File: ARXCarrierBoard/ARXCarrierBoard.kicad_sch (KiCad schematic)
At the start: 24 parts, among them J1 Conn_01x02_Male, J2 Conn_01x03_Male, J3 Conn_02x04_Male, J4 USB_B, SW2 SW_SPST, U2 SeeeduinoXIAO, U3 MAX3485

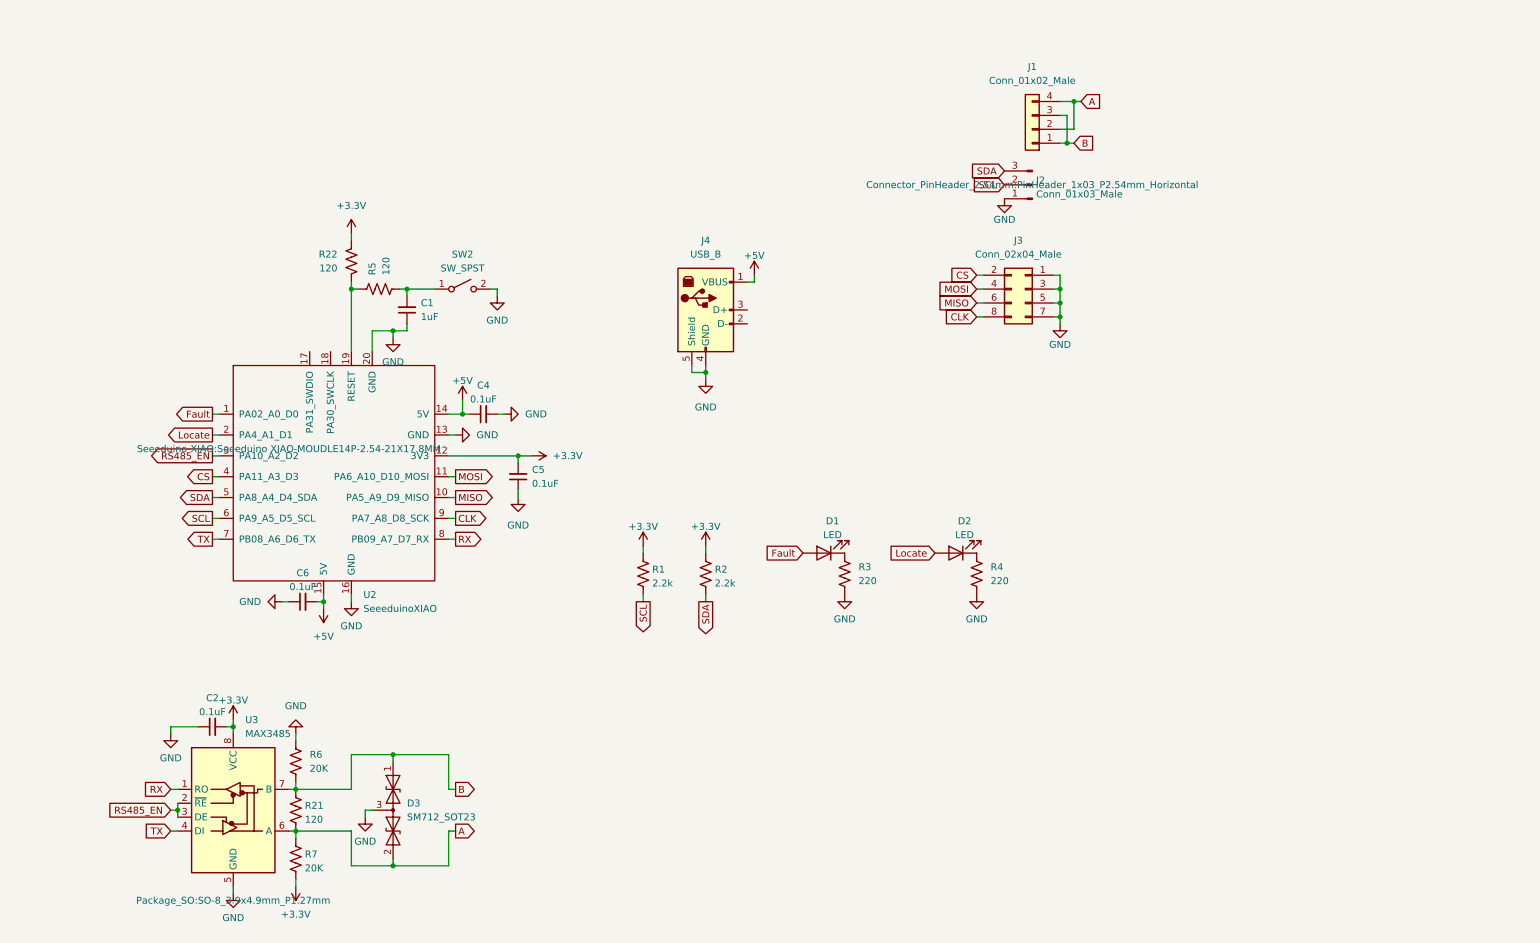
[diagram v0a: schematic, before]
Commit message: Latest version of ARX control board
Updating the board:

- Including new DB9 connector wired to all the control signals.
- Adding the standard SWD port connector to program the microcontroller from scratch.
- Rewiring the order of the pins on some connectors to match the same order on the ARX boards.
- Adding some pull up and pull down resistors.
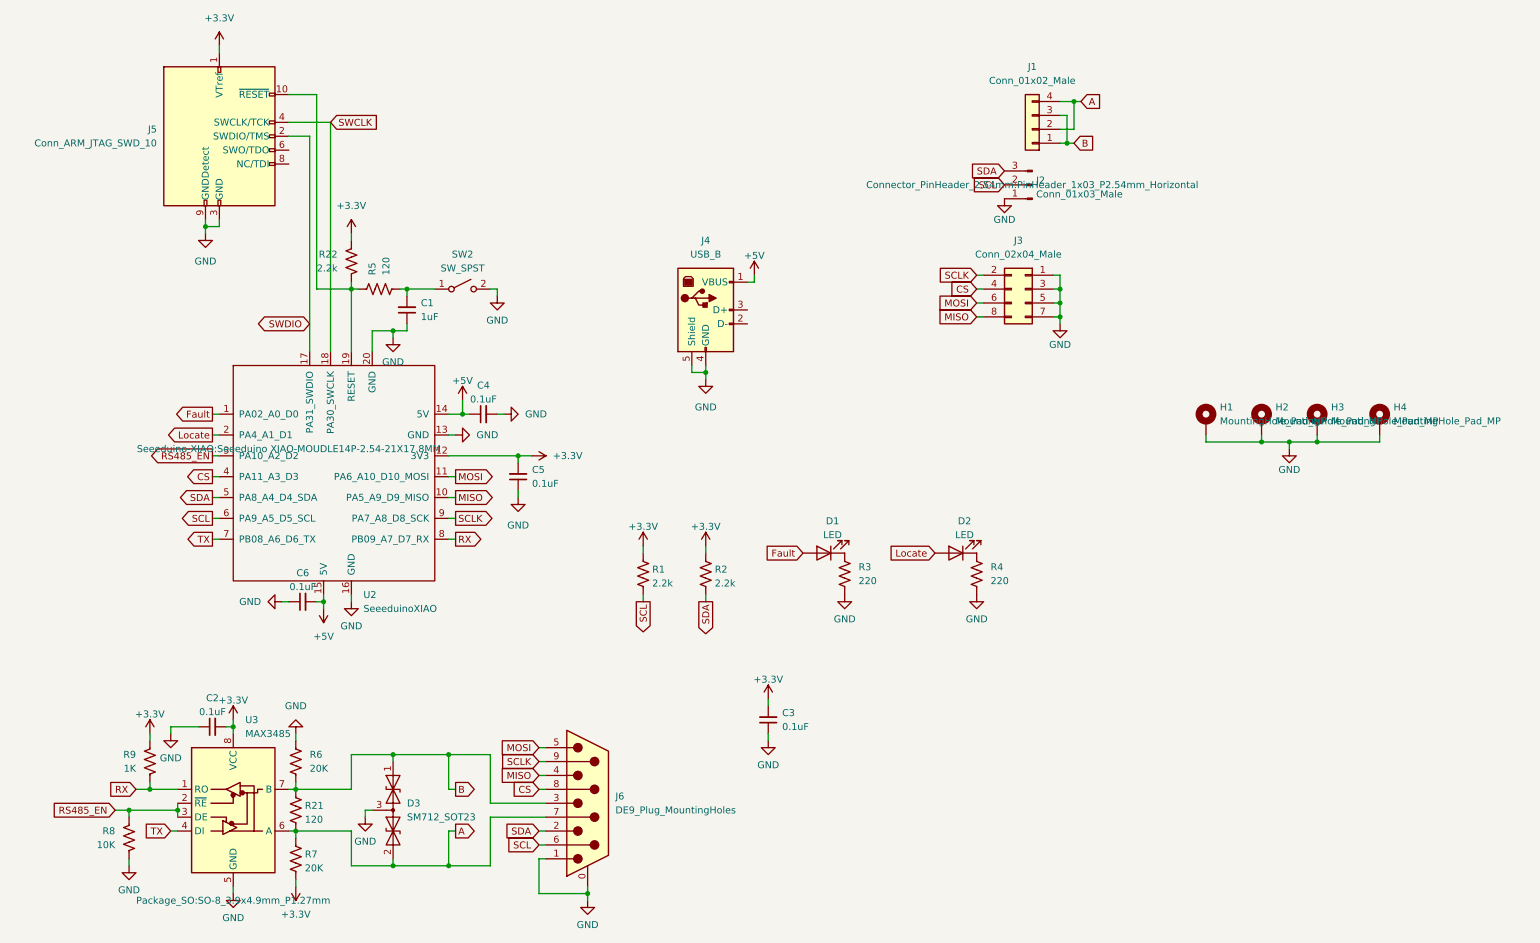
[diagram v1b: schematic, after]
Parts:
- added C3: 0.1uF, Capacitor_SMD:C_1206_3216Metric_Pad1.33x1.80mm_HandSolder, symbol Device:C_Small
- added H1, H2, H3, H4: MountingHole_Pad_MP, MountingHole:MountingHole_3.5mm_Pad_Via, symbol Mechanical:MountingHole_Pad
- added J5: Conn_ARM_JTAG_SWD_10, Connector_PinHeader_1.27mm:PinHeader_2x05_P1.27mm_Vertical, symbol Connector:Conn_ARM_JTAG_SWD_10
- added J6: DE9_Plug_MountingHoles, Connector_Dsub:DSUB-9_Female_Horizontal_P2.77x2.84mm_EdgePinOffset4.94mm_Housed_MountingHolesOffset7.48mm, symbol Connector:DE9_Plug_MountingHoles
- added R8: 10K, Resistor_SMD:R_1206_3216Metric_Pad1.30x1.75mm_HandSolder, symbol Device:R_US
- added R9: 1K, Resistor_SMD:R_1206_3216Metric_Pad1.30x1.75mm_HandSolder, symbol Device:R_US
- R22: value 120 -> 2.2k
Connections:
- net +3.3V: now also C3.2, J5.1 (VTref), R9.1
- net A: now also J6.7
- net B: now also J6.3
- net CS: now also J3.4 (Pin_4), J6.8; no longer J3.2 (Pin_2)
- net GND: now also C3.1, H1.1, H2.1, H3.1, H4.1, J5.3 (GND), J5.5 (GND), J5.9 (GNDDetect), J6.0 (PAD), J6.1, R8.2
- net MISO: now also J3.8 (Pin_8), J6.4; no longer J3.6 (Pin_6)
- net MOSI: now also J3.6 (Pin_6), J6.5; no longer J3.4 (Pin_4)
- net RS485_EN: now also R8.1
- net RX: now also R9.2
- net SCL: now also J6.6
- net SDA: now also J6.2
- net SWDIO: now reaches U2.17 (PA31_SWDIO)
- net SWDIO: now also J5.2 (SWDIO/TMS)
- net SWCLK: now reaches U2.18 (PA30_SWCLK)
- net SWCLK: now also J5.4 (SWCLK/TCK)
- net at R22.1, R5.2, U2.19 (RESET): now also J5.10 (~{RESET})
- net CLK renamed SCLK
- net SCLK: now also J3.2 (Pin_2), J6.9; no longer J3.8 (Pin_8)
